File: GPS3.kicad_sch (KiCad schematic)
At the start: 12 parts, among them J1 GPS_ANT_3, U1 NEO-6M-GPS, U2 24AA32A-I_ST

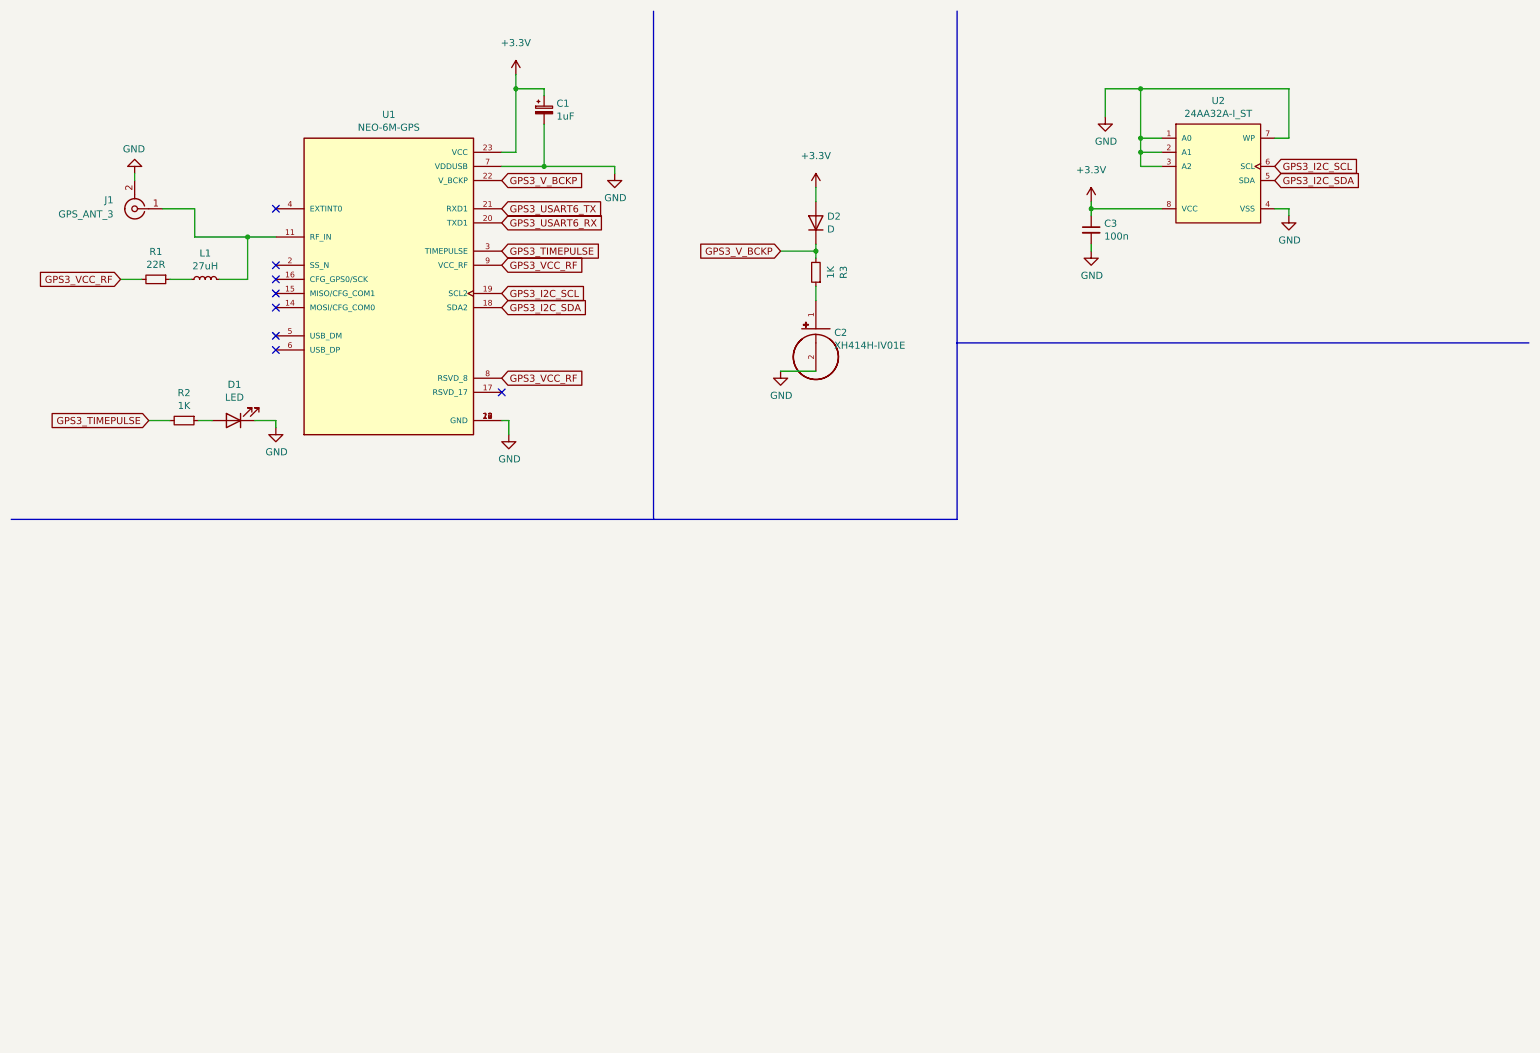
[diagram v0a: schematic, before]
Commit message: Adding M10
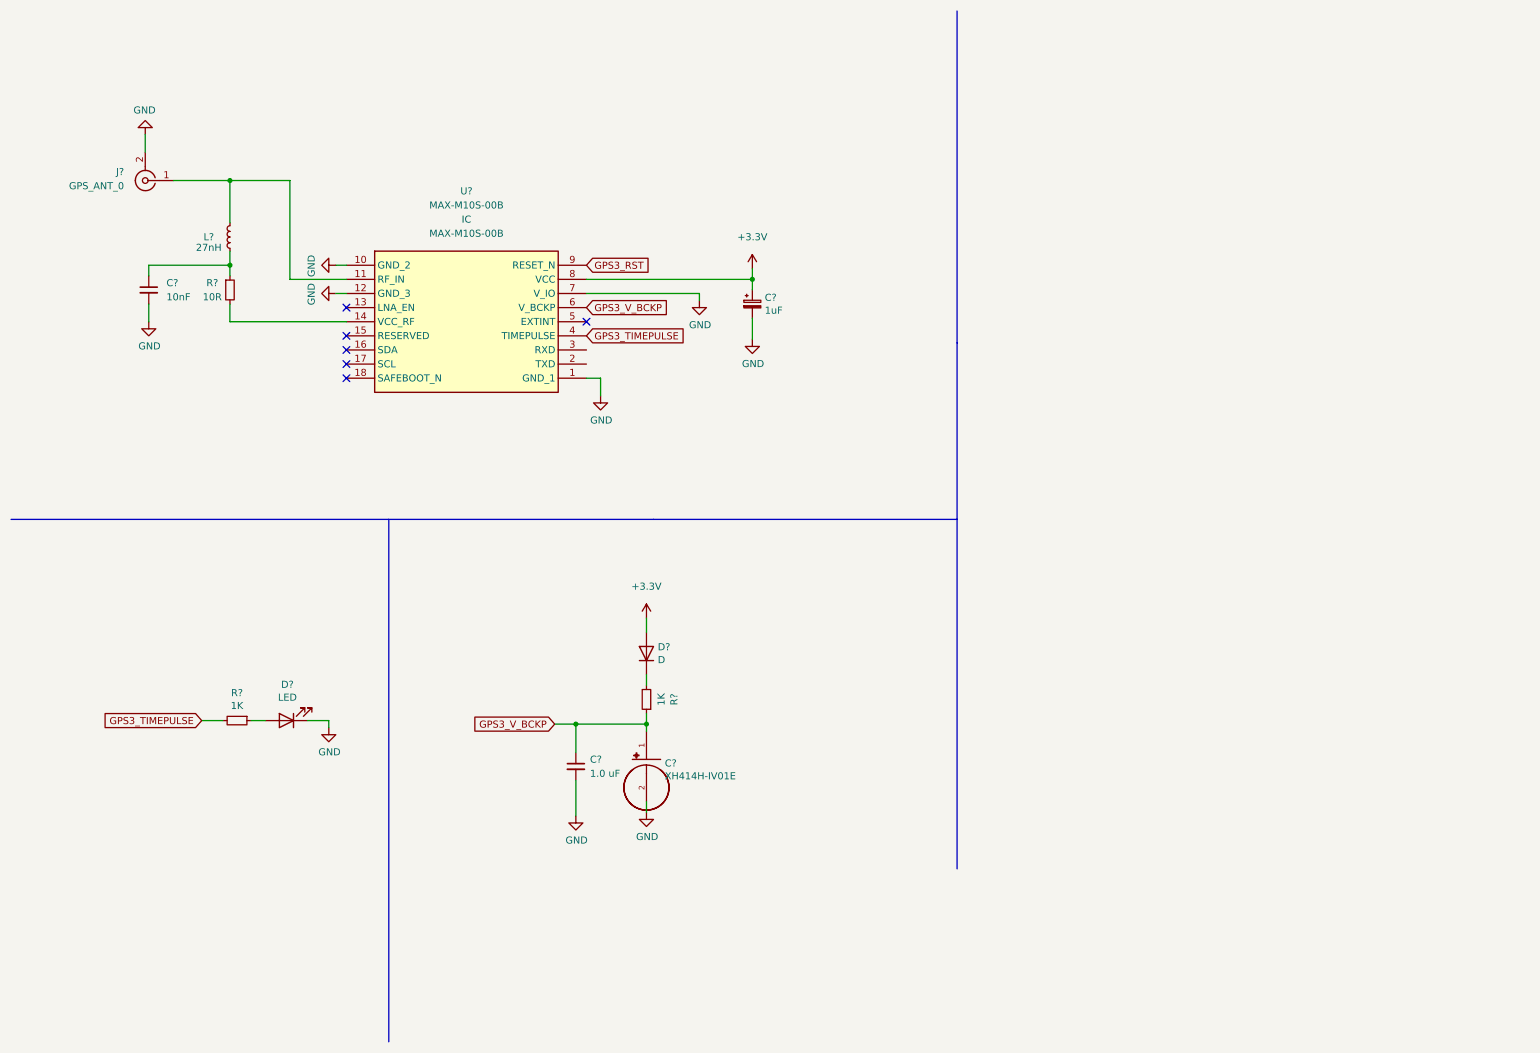
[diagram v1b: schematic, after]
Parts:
- removed C1: 1uF, Capacitor_Tantalum_SMD:CP_EIA-3528-21_Kemet-B_Pad1.50x2.35mm_HandSolder, symbol Device:CP_Small
- removed C2: XH414H-IV01E, XH414H:CAP_XH414H-IV01E, symbol XH414H-IV01E:XH414H-IV01E
- removed C3: 100n, Capacitor_SMD:C_0402_1005Metric, symbol Device:C_Small
- removed D1: LED, LED_SMD:LED_0805_2012Metric_Pad1.15x1.40mm_HandSolder, symbol Device:LED
- removed D2: D, Diode_SMD:D_1206_3216Metric_Pad1.42x1.75mm_HandSolder, symbol Device:D
- removed J1: GPS_ANT_3, Connector_Coaxial:SMA_Samtec_SMA-J-P-X-ST-EM1_EdgeMount, symbol Connector:Conn_Coaxial
- removed L1: 27uH, Inductor_SMD:L_0805_2012Metric, symbol Device:L_Small
- removed R1: 22R, Resistor_SMD:R_0805_2012Metric, symbol Device:R_Small
- removed R2, R3: 1K, Resistor_SMD:R_0805_2012Metric, symbol Device:R_Small
- removed U1: NEO-6M-GPS, NEO 6M:XCVR_NEO-6M-GPS, symbol NEO-6M-GPS:NEO-6M-GPS
- removed U2: 24AA32A-I_ST, 24AA32A-I_ST:SOP65P640X120-8N, symbol eec:24AA32A-I_ST
- added C?: 1uF, Capacitor_Tantalum_SMD:CP_EIA-3528-21_Kemet-B_Pad1.50x2.35mm_HandSolder, symbol Device:CP_Small
- added C?: 1.0 uF, Capacitor_SMD:C_0805_2012Metric, symbol Device:C_Small
- added C?: XH414H-IV01E, XH414H:CAP_XH414H-IV01E, symbol XH414H-IV01E:XH414H-IV01E
- added C?: 10nF, Capacitor_SMD:C_0805_2012Metric, symbol Device:C_Small
- added D?: D, Diode_SMD:D_1206_3216Metric_Pad1.42x1.75mm_HandSolder, symbol Device:D
- added D?: LED, LED_SMD:LED_0805_2012Metric_Pad1.15x1.40mm_HandSolder, symbol Device:LED
- added J?: GPS_ANT_0, Connector_Coaxial:SMA_Samtec_SMA-J-P-X-ST-EM1_EdgeMount, symbol Connector:Conn_Coaxial
- added L?: 27nH, Inductor_SMD:L_0805_2012Metric, symbol Device:L_Small
- added R? (x2): 1K, Resistor_SMD:R_0805_2012Metric, symbol Device:R_Small
- added R?: 10R, Resistor_SMD:R_0805_2012Metric, symbol Device:R_Small
- added U?: MAX-M10S-00B, MAX-M10S-00B:MAXM10S00B, symbol MAX-M10S-00B:MAX-M10S-00B
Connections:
- net +3.3V: now also C?.1, D?.2 (A), U?.8 (VCC)
- net GND: now also C?.2, C?.2, C?.2, C?.2, D?.1 (K), J?.2 (Ext), U?.1 (GND_1), U?.10 (GND_2), U?.12 (GND_3), U?.7 (V_IO)
- net GPS3_TIMEPULSE: now also R?.2, U?.4 (TIMEPULSE)
- net GPS3_V_BCKP: now also C?.1, C?.1, R?.1, U?.6 (V_BCKP)
- new net: D?.2 (A), R?.1
- new net: D?.1 (K), R?.2
- new net: J?.1 (In), L?.2, U?.11 (RF_IN)
- new net: R?.2, U?.14 (VCC_RF)
- new net: C?.1, L?.1, R?.1
- new net GPS3_RST: U?.9 (RESET_N)
- no-connect marks 8 -> 6

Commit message: Finished M10
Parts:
- C9: renamed from C?; footprint Capacitor_SMD:C_0805_2012Metric -> Capacitor_SMD:C_0402_1005Metric
- L4: renamed from L?; footprint Inductor_SMD:L_0805_2012Metric -> Inductor_SMD:L_0402_1005Metric
- R7: renamed from R?; footprint Resistor_SMD:R_0805_2012Metric -> Resistor_SMD:R_0402_1005Metric
- gave numbers to parts that had none: 9
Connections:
- net GPS3_USART2_RX: now reaches U3.2 (TXD)
- net GPS3_USART2_TX: now reaches U3.3 (RXD)
- net GPS3_RST renamed GPS3_RESET
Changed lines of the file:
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@@
     (stroke (width 0) (type default) (color 0 0 0 0))
   )
-  (global_label "GPS3_RST" (shape input) (at 115.57 57.785 0) (fields_autoplaced)
+  (global_label "GPS3_USART2_RX" (shape input) (at 115.57 75.565 0) (fields_autoplaced)
     (effects (font (size 1.27 1.27)) (justify left))
-    (property "Intersheet References" "${INTERSHEET_REFS}" (id 0) (at 127.3569 57.7056 0)
+    (property "Intersheet References" "${INTERSHEET_REFS}" (id 0) (at 134.4326 75.4856 0)
       (effects (font (size 1.27 1.27)) (justify left) hide)
     )
@@
     )
   )
+  (global_label "GPS3_RESET" (shape input) (at 115.57 57.785 0) (fields_autoplaced)
+    (effects (font (size 1.27 1.27)) (justify left))
+    (property "Intersheet References" "${INTERSHEET_REFS}" (id 0) (at 129.655 57.7056 0)
+      (effects (font (size 1.27 1.27)) (justify left) hide)
+    )
+  )
   (global_label "GPS3_V_BCKP" (shape input) (at 109.855 140.335 180) (fields_autoplaced)
     (effects (font (size 1.27 1.27)) (justify right))
@@
     )
   )
+  (global_label "GPS3_USART2_TX" (shape input) (at 115.57 73.025 0) (fields_autoplaced)
+    (effects (font (size 1.27 1.27)) (justify left))
+    (property "Intersheet References" "${INTERSHEET_REFS}" (id 0) (at 134.1302 72.9456 0)
+      (effects (font (size 1.27 1.27)) (justify left) hide)
+    )
+  )
   (symbol (lib_id "Device:CP_Small") (at 145.415 64.77 0) (unit 1)
     (in_bom yes) (on_board yes)
-    (property "Reference" "C?" (id 0) (at 147.6502 63.6016 0)
+    (property "Reference" "C24" (id 0) (at 147.6502 63.6016 0)
       (effects (font (size 1.27 1.27)) (justify left))
     )
@@
   (symbol (lib_id "Device:R_Small") (at 52.705 139.7 270) (unit 1)
     (in_bom yes) (on_board yes)
-    (property "Reference" "R?" (id 0) (at 52.705 134.7216 90))
+    (property "Reference" "R8" (id 0) (at 52.705 134.7216 90))
     (property "Value" "1K" (id 1) (at 52.705 137.033 90))
     (property "Footprint" "Resistor_SMD:R_0805_2012Metric" (id 2) (at 52.705 139.7 0)
@@
   (symbol (lib_id "power:GND") (at 135.89 64.135 0) (unit 1)
     (in_bom yes) (on_board yes)
-    (property "Reference" "#PWR?" (id 0) (at 135.89 70.485 0)
+    (property "Reference" "#PWR097" (id 0) (at 135.89 70.485 0)
       (effects (font (size 1.27 1.27)) hide)
     )
@@
   (symbol (lib_id "power:GND") (at 118.11 81.28 0) (unit 1)
     (in_bom yes) (on_board yes)
-    (property "Reference" "#PWR?" (id 0) (at 118.11 87.63 0)
+    (property "Reference" "#PWR094" (id 0) (at 118.11 87.63 0)
       (effects (font (size 1.27 1.27)) hide)
     )
@@
   (symbol (lib_id "power:GND") (at 69.215 140.97 0) (unit 1)
     (in_bom yes) (on_board yes)
-    (property "Reference" "#PWR?" (id 0) (at 69.215 147.32 0)
+    (property "Reference" "#PWR090" (id 0) (at 69.215 147.32 0)
       (effects (font (size 1.27 1.27)) hide)
     )
@@
   (symbol (lib_id "power:GND") (at 36.83 67.945 0) (unit 1)
     (in_bom yes) (on_board yes)
-    (property "Reference" "#PWR?" (id 0) (at 36.83 74.295 0)
+    (property "Reference" "#PWR089" (id 0) (at 36.83 74.295 0)
       (effects (font (size 1.27 1.27)) hide)
     )
@@
   (symbol (lib_id "power:+3.3V") (at 126.365 121.285 0) (unit 1)
     (in_bom yes) (on_board yes) (fields_autoplaced)
-    (property "Reference" "#PWR?" (id 0) (at 126.365 125.095 0)
+    (property "Reference" "#PWR095" (id 0) (at 126.365 125.095 0)
       (effects (font (size 1.27 1.27)) hide)
     )
@@
   (symbol (lib_id "Device:R_Small") (at 126.365 135.89 180) (unit 1)
     (in_bom yes) (on_board yes)
-    (property "Reference" "R?" (id 0) (at 131.3434 135.89 90))
+    (property "Reference" "R9" (id 0) (at 131.3434 135.89 90))
     (property "Value" "1K" (id 1) (at 129.032 135.89 90))
     (property "Footprint" "Resistor_SMD:R_0805_2012Metric" (id 2) (at 126.365 135.89 0)
@@
   (symbol (lib_id "power:GND") (at 126.365 156.21 0) (unit 1)
     (in_bom yes) (on_board yes)
-    (property "Reference" "#PWR?" (id 0) (at 126.365 162.56 0)
+    (property "Reference" "#PWR096" (id 0) (at 126.365 162.56 0)
       (effects (font (size 1.27 1.27)) hide)
     )
@@
   (symbol (lib_id "MAX-M10S-00B:MAX-M10S-00B") (at 72.39 57.785 0) (unit 1)
     (in_bom yes) (on_board yes) (fields_autoplaced)
-    (property "Reference" "U?" (id 0) (at 93.98 44.45 0))
+    (property "Reference" "U3" (id 0) (at 93.98 44.45 0))
     (property "Value" "MAX-M10S-00B" (id 1) (at 93.98 46.99 0))
     (property "Footprint" "MAX-M10S-00B:MAXM10S00B" (id 2) (at 72.39 57.785 0)
@@
   (symbol (lib_id "power:+3.3V") (at 145.415 58.42 0) (unit 1)
     (in_bom yes) (on_board yes) (fields_autoplaced)
-    (property "Reference" "#PWR?" (id 0) (at 145.415 62.23 0)
+    (property "Reference" "#PWR098" (id 0) (at 145.415 62.23 0)
       (effects (font (size 1.27 1.27)) hide)
     )
@@
   (symbol (lib_id "Device:R_Small") (at 51.435 62.23 0) (unit 1)
     (in_bom yes) (on_board yes)
-    (property "Reference" "R?" (id 0) (at 48.26 60.96 0))
+    (property "Reference" "R7" (id 0) (at 48.26 60.96 0))
     (property "Value" "10R" (id 1) (at 48.26 63.5 0))
-    (property "Footprint" "Resistor_SMD:R_0805_2012Metric" (id 2) (at 51.435 62.23 0)
+    (property "Footprint" "Resistor_SMD:R_0402_1005Metric" (id 2) (at 51.435 62.23 0)
       (effects (font (size 1.27 1.27)) hide)
     )
@@
   (symbol (lib_id "Device:C_Small") (at 113.665 147.955 0) (unit 1)
     (in_bom yes) (on_board yes) (fields_autoplaced)
-    (property "Reference" "C?" (id 0) (at 116.205 146.6912 0)
+    (property "Reference" "C22" (id 0) (at 116.205 146.6912 0)
       (effects (font (size 1.27 1.27)) (justify left))
     )
@@
   (symbol (lib_id "power:GND") (at 36.195 34.29 180) (unit 1)
     (in_bom yes) (on_board yes)
-    (property "Reference" "#PWR?" (id 0) (at 36.195 27.94 0)
+    (property "Reference" "#PWR051" (id 0) (at 36.195 27.94 0)
       (effects (font (size 1.27 1.27)) hide)
     )
@@
   (symbol (lib_id "Device:L_Small") (at 51.435 52.705 180) (unit 1)
     (in_bom yes) (on_board yes)
-    (property "Reference" "L?" (id 0) (at 47.625 52.705 0))
+    (property "Reference" "L4" (id 0) (at 47.625 52.705 0))
     (property "Value" "27nH" (id 1) (at 47.625 54.61 0))
-    (property "Footprint" "Inductor_SMD:L_0805_2012Metric" (id 2) (at 51.435 52.705 0)
+    (property "Footprint" "Inductor_SMD:L_0402_1005Metric" (id 2) (at 51.435 52.705 0)
       (effects (font (size 1.27 1.27)) hide)
     )
@@
   (symbol (lib_id "power:GND") (at 70.485 62.865 270) (unit 1)
     (in_bom yes) (on_board yes)
-    (property "Reference" "#PWR?" (id 0) (at 64.135 62.865 0)
+    (property "Reference" "#PWR092" (id 0) (at 64.135 62.865 0)
       (effects (font (size 1.27 1.27)) hide)
     )
@@
   (symbol (lib_id "XH414H-IV01E:XH414H-IV01E") (at 126.365 146.685 0) (unit 1)
     (in_bom yes) (on_board yes)
-    (property "Reference" "C?" (id 0) (at 129.667 147.3708 0)
+    (property "Reference" "C23" (id 0) (at 129.667 147.3708 0)
       (effects (font (size 1.27 1.27)) (justify left))
     )
@@
   (symbol (lib_id "Device:C_Small") (at 36.83 62.23 0) (unit 1)
     (in_bom yes) (on_board yes) (fields_autoplaced)
-    (property "Reference" "C?" (id 0) (at 40.005 60.9662 0)
+    (property "Reference" "C9" (id 0) (at 40.005 60.9662 0)
       (effects (font (size 1.27 1.27)) (justify left))
     )
@@
       (effects (font (size 1.27 1.27)) (justify left))
     )
-    (property "Footprint" "Capacitor_SMD:C_0805_2012Metric" (id 2) (at 36.83 62.23 0)
+    (property "Footprint" "Capacitor_SMD:C_0402_1005Metric" (id 2) (at 36.83 62.23 0)
       (effects (font (size 1.27 1.27)) hide)
     )
@@
   (symbol (lib_id "power:GND") (at 145.415 71.12 0) (unit 1)
     (in_bom yes) (on_board yes)
-    (property "Reference" "#PWR?" (id 0) (at 145.415 77.47 0)
+    (property "Reference" "#PWR099" (id 0) (at 145.415 77.47 0)
       (effects (font (size 1.27 1.27)) hide)
     )
@@
   (symbol (lib_id "Connector:Conn_Coaxial") (at 36.195 42.545 180) (unit 1)
     (in_bom yes) (on_board yes)
-    (property "Reference" "J?" (id 0) (at 32.385 40.9817 0)
+    (property "Reference" "J3" (id 0) (at 32.385 40.9817 0)
       (effects (font (size 1.27 1.27)) (justify left))
     )
@@
   (symbol (lib_id "Device:D") (at 126.365 127.635 90) (unit 1)
     (in_bom yes) (on_board yes)
-    (property "Reference" "D?" (id 0) (at 128.397 126.4666 90)
+    (property "Reference" "D9" (id 0) (at 128.397 126.4666 90)
       (effects (font (size 1.27 1.27)) (justify right))
     )
@@
   (symbol (lib_id "power:GND") (at 70.485 57.785 270) (unit 1)
     (in_bom yes) (on_board yes)
-    (property "Reference" "#PWR?" (id 0) (at 64.135 57.785 0)
+    (property "Reference" "#PWR091" (id 0) (at 64.135 57.785 0)
       (effects (font (size 1.27 1.27)) hide)
     )
@@
   (symbol (lib_id "Device:LED") (at 61.595 139.7 180) (unit 1)
     (in_bom yes) (on_board yes)
-    (property "Reference" "D?" (id 0) (at 61.7728 133.223 0))
+    (property "Reference" "D8" (id 0) (at 61.7728 133.223 0))
     (property "Value" "LED" (id 1) (at 61.7728 135.5344 0))
     (property "Footprint" "LED_SMD:LED_0805_2012Metric_Pad1.15x1.40mm_HandSolder" (id 2) (at 61.595 139.7 0)
@@
   (symbol (lib_id "power:GND") (at 113.665 156.845 0) (unit 1)
     (in_bom yes) (on_board yes)
-    (property "Reference" "#PWR?" (id 0) (at 113.665 163.195 0)
-      (effects (font (size 1.27 1.27)) hide)
-    )
+    (property "Reference" "#PWR093" (id 0) (at 113.665 163.195 0)
+      (effects (font (size 1.27 1.27)) hide)
+    )
